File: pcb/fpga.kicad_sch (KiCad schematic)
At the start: 38 parts, among them J3 SBH11-PBPC-D05-ST-BK, J5 PINHD-1x7_ONIXJTAG-RevA, SW1 R-668049, U11 W25Q80EWUXIE, U12 DSC6011JI1A-050.0000, U8 LIF-MD6000-6UMG64I

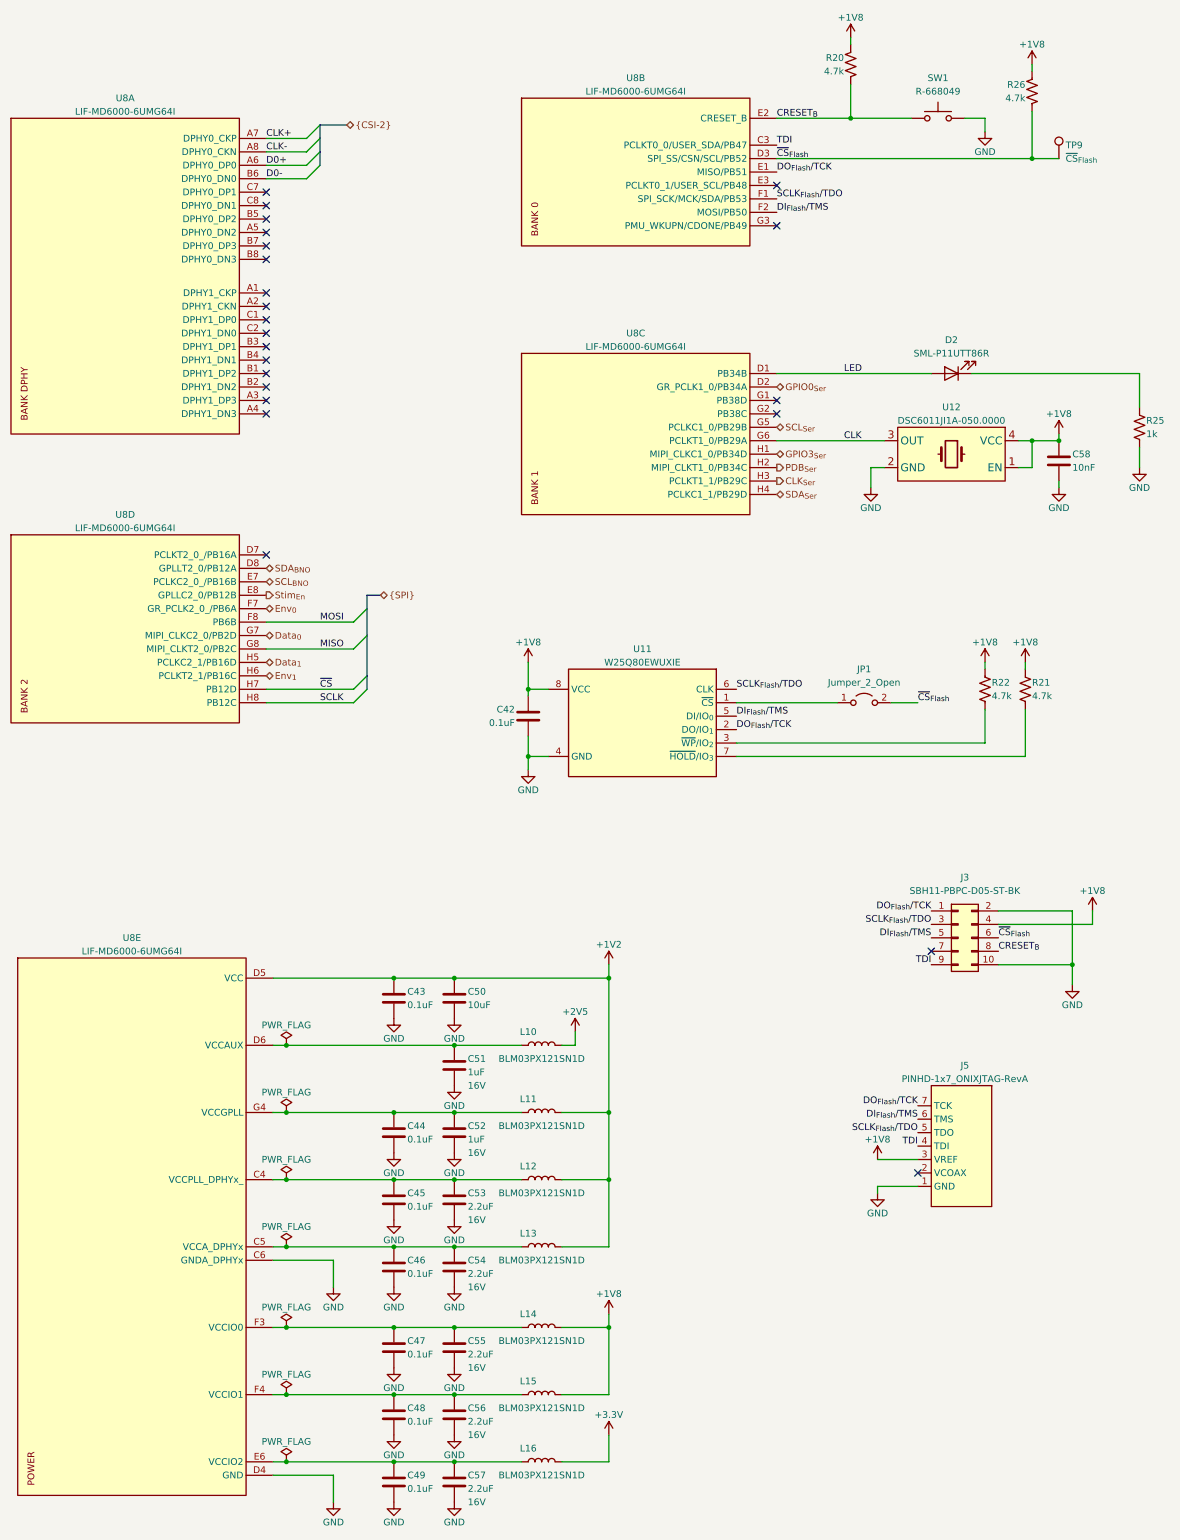
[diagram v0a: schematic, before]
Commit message: Revision B
- Bring in changes from headstage-rhs116 rev. C that should make this design
  fully functional
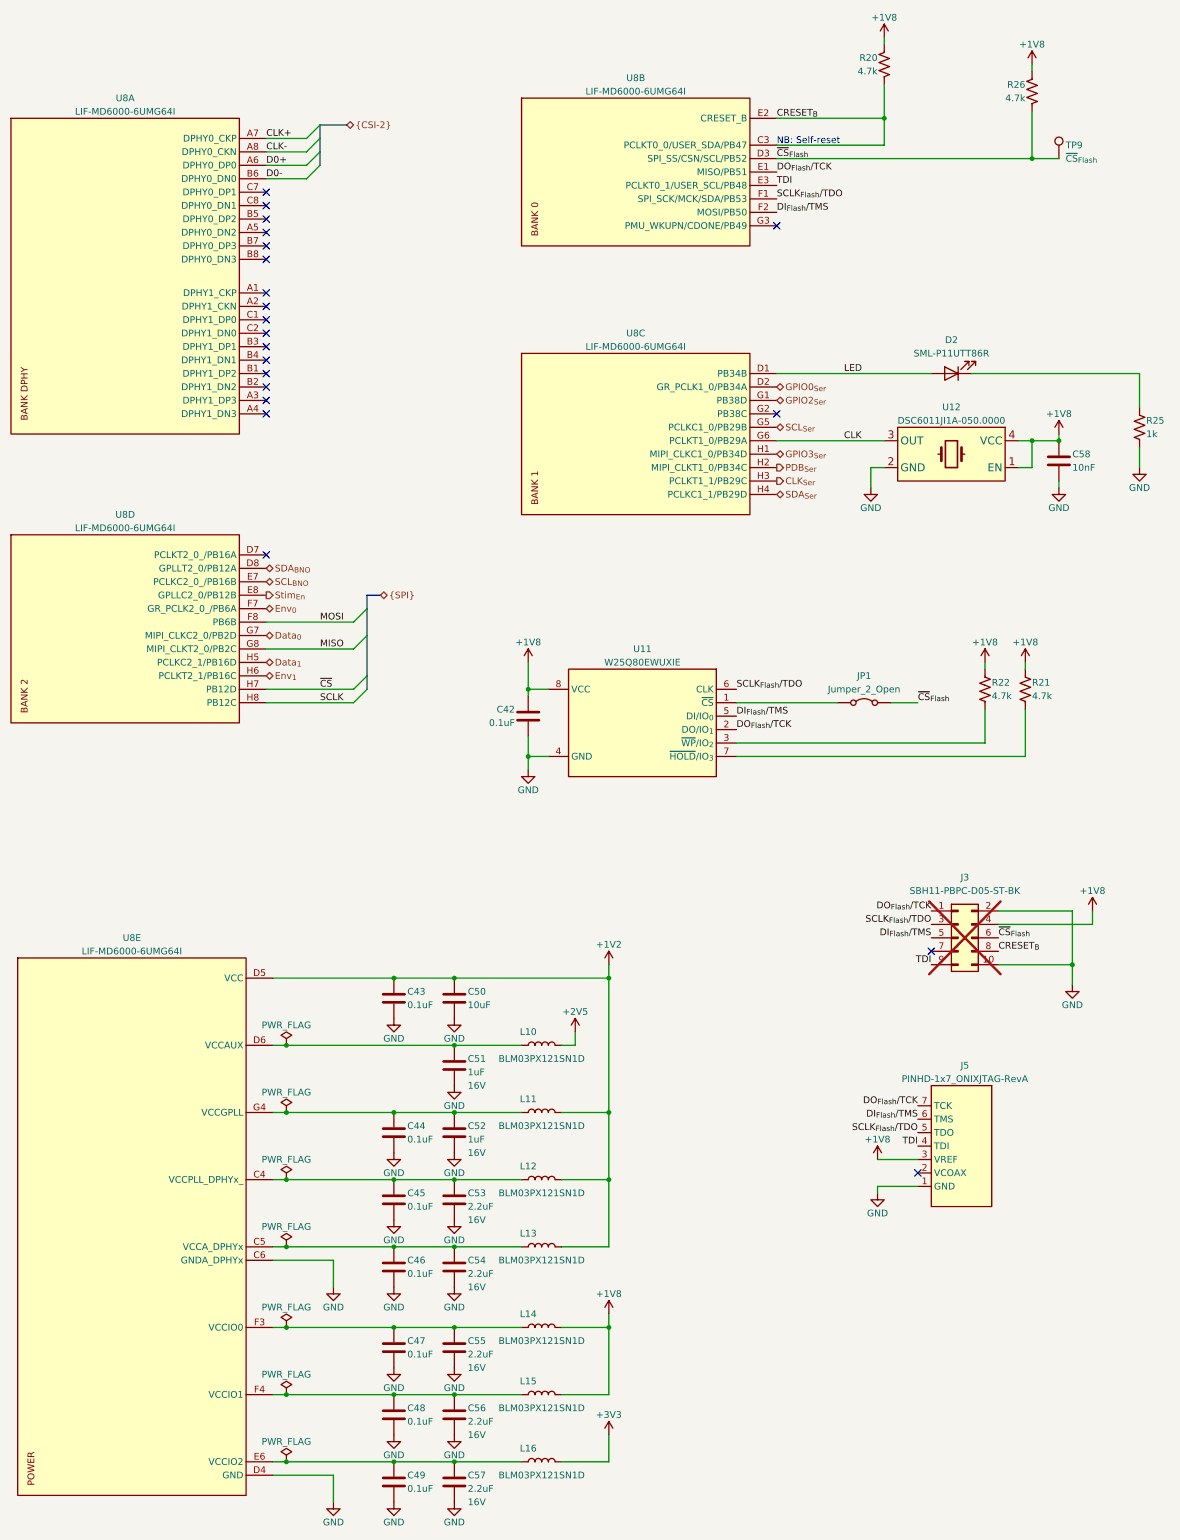
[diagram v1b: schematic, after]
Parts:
- removed SW1: R-668049, jonnew:MITSUMI_R-668049, symbol Switch:SW_Push
- J3: now not fitted
- JP1: symbol Jumper:Jumper_2_Open -> Jumper:Jumper_2_Bridged; now in the parts list
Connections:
- net CRESET_{B}: now also U8.C3 (PCLKT0_0/USER_SDA/PB47)
- net TDI: now also U8.E3 (PCLKT0_1/USER_SCL/PB48); no longer U8.C3 (PCLKT0_0/USER_SDA/PB47)
- net GPIO2_{Ser}: now reaches U8.G1 (PB38D)
- no-connect marks 23 -> 21
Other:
- note added: "NB: Self-reset"
- moved on the sheet: R20
